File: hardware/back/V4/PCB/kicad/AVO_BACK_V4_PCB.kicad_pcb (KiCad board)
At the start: 4 copper layers, 46.7 x 47.4 mm, 105 parts, among them J1 USB-C 16P, J2 BATERÍA 1S, J3 microSD DM3AT, J4 URTK1.2 (8 hilos), Q1 AO3401A, Q2 AO3401A, Q3 AO3401A, Q4 AO3401A, U1 BQ51013BRHLR, U2 BQ24072RGTR, U3 TLV75733PDBVR, U4 ESP32-S3-MINI-1U-N8, U6 USBLC6-2SC6, U7 RT9080-33GJ5, U8 DRV5032FADBZR

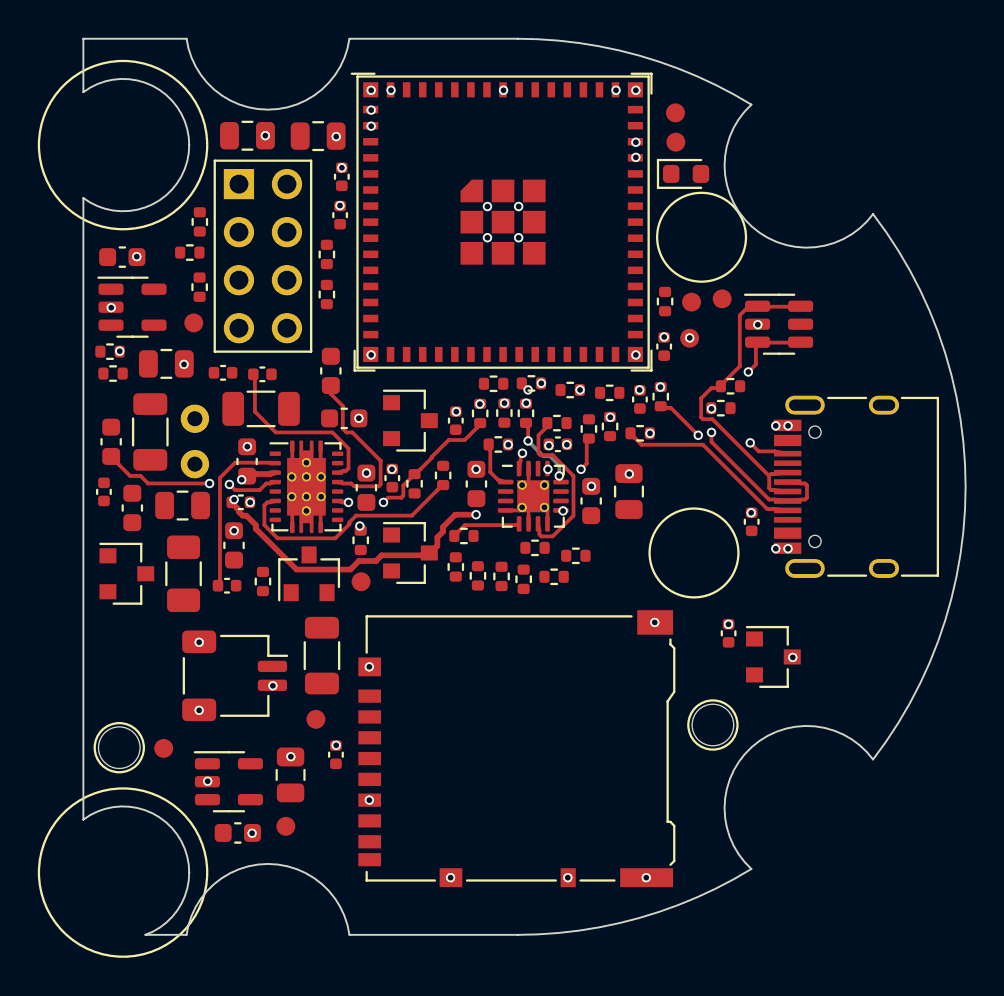
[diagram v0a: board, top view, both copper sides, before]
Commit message: PCB espalda V4: resultados de KiCad 9 de f2d8330 (puerta: false) [skip ci]
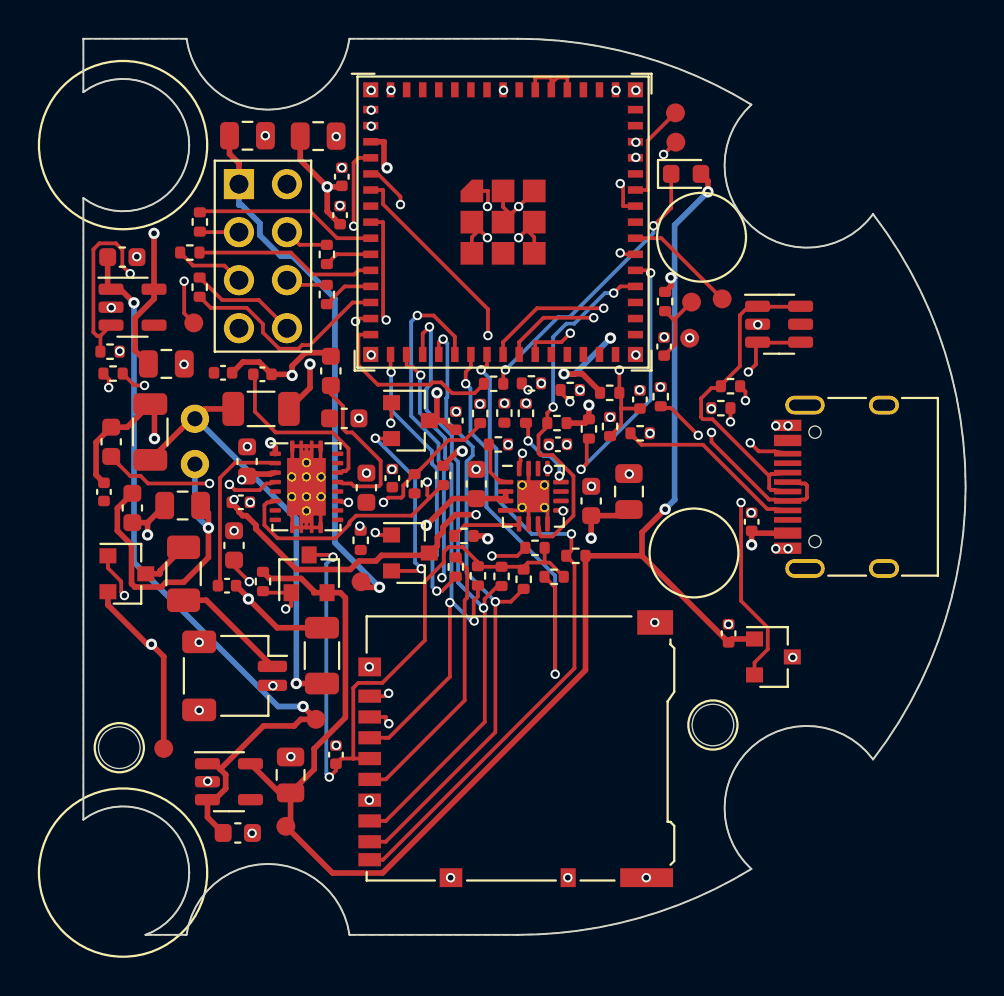
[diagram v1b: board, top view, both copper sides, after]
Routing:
- net +3V3: track 0.00 -> 136.9 mm, vias 0 -> 7
- net VBAT: track 0.00 -> 71.7 mm, vias 0 -> 4
- net VSYS: track 0.00 -> 65.0 mm, vias 0 -> 4
- net QI_AC1: track 0.00 -> 46.4 mm, vias 0 -> 5
- net +3V3_SD: track 0.00 -> 44.4 mm, vias 0 -> 3
- net HALL: track 0.00 -> 43.8 mm, vias 0 -> 2
- net +3V3_ZED: track 0.00 -> 41.9 mm, vias 0 -> 2
- net SD_PWR_N: track 0.00 -> 41.4 mm, vias 0 -> 2
- net SD_D3: track 0.00 -> 35.5 mm, vias 0 -> 3
- net SD_CD: track 0.00 -> 35.3 mm, vias 0 -> 2
- net BAT_G: track 0.00 -> 34.6 mm, vias 0 -> 2
- net SD_D1: track 0.00 -> 34.0 mm, vias 0 -> 2
- net SD_D0: track 0.00 -> 33.8 mm, vias 0 -> 2
- net SD_D2: track 0.00 -> 32.0 mm, vias 0 -> 4
- net QI_AC2: track 0.00 -> 30.5 mm, vias 0 -> 2
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- added copper zone on In2.Cu, net +3V3
- added copper zone on B.Cu, net GND
- added copper zone on F.Cu, net GND

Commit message: PCB espalda V4: resultados de KiCad 9 de 04e2e6f (puerta: false) [skip ci]
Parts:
- moved TP2 26.9 mm to (96.7, 81.8)
- moved TP9 22.9 mm to (99.4, 92.3)
- moved C62 20.8 mm to (90.1, 95.1)
- moved R47 17.9 mm to (79.0, 116.2), turned to 90 degrees
- moved R4 15.6 mm to (69.2, 99.5), turned to 0 degrees
- moved R2 15.5 mm to (74.8, 106.0), turned to 0 degrees
- moved TP7 15.0 mm to (67.0, 99.2)
- moved R54 14.3 mm to (81.3, 77.5)
- moved C8 14.0 mm to (80.7, 102.2)
- moved C61 12.7 mm to (74.2, 81.4)
- moved C11 12.7 mm to (80.0, 104.6), turned to 90 degrees
- moved C5 12.3 mm to (79.0, 95.2)
- moved C4 11.0 mm to (81.9, 99.6)
- moved C40 9.15 mm to (78.0, 111.2)
- moved RT1 9.06 mm to (85.8, 104.9), turned to 0 degrees
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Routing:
- net +3V3: track 136.9 -> 0.00 mm, vias 7 -> 0
- net VBAT: track 71.7 -> 0.00 mm, vias 4 -> 0
- net VSYS: track 65.0 -> 0.00 mm, vias 4 -> 0
- net QI_AC1: track 46.4 -> 0.00 mm, vias 5 -> 0
- net +3V3_SD: track 44.4 -> 0.00 mm, vias 3 -> 0
- net HALL: track 43.8 -> 0.00 mm, vias 2 -> 0
- net +3V3_ZED: track 41.9 -> 0.00 mm, vias 2 -> 0
- net SD_PWR_N: track 41.4 -> 0.00 mm, vias 2 -> 0
- net SD_D3: track 35.5 -> 0.00 mm, vias 3 -> 0
- net SD_CD: track 35.3 -> 0.00 mm, vias 2 -> 0
- net BAT_G: track 34.6 -> 0.00 mm, vias 2 -> 0
- net SD_D1: track 34.0 -> 0.00 mm, vias 2 -> 0
- net SD_D0: track 33.8 -> 0.00 mm, vias 2 -> 0
- net SD_D2: track 32.0 -> 0.00 mm, vias 4 -> 0
- net QI_AC2: track 30.5 -> 0.00 mm, vias 2 -> 0
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- removed copper zone on In2.Cu, net +3V3
- removed copper zone on B.Cu, net GND
- removed copper zone on F.Cu, net GND
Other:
- outline, holes or cut-outs redrawn

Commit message: PCB espalda V4: resultados de KiCad 9 de a08bbd6 (puerta: false) [skip ci]
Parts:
- moved TP2 26.9 mm to (71.5, 91.3)
- moved TP9 22.9 mm to (80.4, 105.0)
- moved C62 20.8 mm to (74.4, 81.4)
- moved R47 17.9 mm to (91.8, 103.7), turned to 0 degrees
- moved R4 15.6 mm to (84.7, 99.4), turned to 90 degrees
- moved R2 15.5 mm to (86.7, 96.1), turned to 90 degrees
- moved TP7 15.0 mm to (70.0, 113.8)
- moved R54 14.3 mm to (71.3, 87.6)
- moved C8 14.0 mm to (66.8, 100.3)
- moved C61 12.7 mm to (70.1, 93.5)
- moved C11 12.7 mm to (73.1, 94.0), turned to 0 degrees
- moved C5 12.3 mm to (68.3, 101.1)
- moved C4 11.0 mm to (71.0, 101.0)
- moved C40 9.15 mm to (73.7, 103.1)
- moved RT1 9.06 mm to (88.0, 96.1), turned to 90 degrees
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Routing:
- net +3V3: track 0.00 -> 138.4 mm, vias 0 -> 7
- net VSYS: track 0.00 -> 60.8 mm, vias 0 -> 4
- net +3V3_ZED: track 0.00 -> 55.7 mm, vias 0 -> 2
- net BAT_G: track 0.00 -> 52.8 mm, vias 0 -> 2
- net VBAT: track 0.00 -> 50.6 mm, vias 0 -> 3
- net VBUS: track 0.00 -> 49.6 mm, vias 0 -> 6
- net QI_AC2: track 0.00 -> 49.5 mm, vias 0 -> 1
- net SD_CD: track 0.00 -> 40.0 mm, vias 0 -> 3
- net QI_CHG: track 7.71 -> 46.6 mm, vias 0 -> 5
- net QI_AC1: track 0.00 -> 38.6 mm, vias 0 -> 3
- net HALL: track 0.00 -> 38.3 mm, vias 0 -> 3
- net +3V3_SD: track 0.00 -> 37.0 mm, vias 0 -> 2
- net SD_CLK0: track 0.00 -> 35.3 mm, vias 0 -> 4
- net SD_D3: track 0.00 -> 34.8 mm, vias 0 -> 4
- net SD_D1: track 0.00 -> 33.4 mm, vias 0 -> 2
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- added copper zone on In2.Cu, net +3V3
- added copper zone on B.Cu, net GND
- added copper zone on F.Cu, net GND

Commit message: PCB espalda V4: resultados de KiCad 9 de 7ee8318 (puerta: false) [skip ci]
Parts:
- moved C40 19.2 mm to (91.6, 96.3)
- moved TP9 17.0 mm to (67.1, 94.5)
- moved C7 15.3 mm to (78.8, 107.5), turned to -90 degrees
- moved R40 14.3 mm to (86.6, 96.4)
- moved C8 14.1 mm to (79.9, 105.4), turned to 0 degrees
- moved Q4 13.9 mm to (88.9, 96.5)
- moved C3 12.3 mm to (69.0, 101.0)
- moved TP7 11.8 mm to (66.9, 102.5)
- moved R55 11.6 mm to (78.5, 96.9), turned to 90 degrees
- moved R43 11.5 mm to (78.5, 109.7), turned to 0 degrees
- moved R41 11.1 mm to (75.6, 103.1)
- moved R53 9.59 mm to (76.7, 94.3)
- moved C11 8.54 mm to (81.5, 95.1), turned to 90 degrees
- moved R6 8.34 mm to (81.5, 97.2), turned to 90 degrees
- moved TP8 7.74 mm to (70.4, 113.9)
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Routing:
- net VBAT: track 50.6 -> 84.5 mm, vias 3 -> 7
- net VIN5: track 27.4 -> 60.1 mm, vias 3 -> 5
- net QI_AC2: track 49.5 -> 20.5 mm, vias 1 -> 2
- net +3V3_ZED: track 55.7 -> 28.2 mm, vias 2 -> 0
- net +3V3: track 138.4 -> 112.9 mm
- net SD_PWR_N: track 32.6 -> 7.59 mm
- net SD_CLK0: track 35.3 -> 18.7 mm, vias 4 -> 2
- net QI_CHG: track 46.6 -> 30.1 mm, vias 5 -> 3
- net +3V3_SD: track 37.0 -> 53.2 mm, vias 2 -> 5
- net QI_ADEN: track 22.2 -> 7.86 mm, vias 2 -> 0
- net BAT_G: track 52.8 -> 38.7 mm
- net QI_RECT: track 3.02 -> 16.2 mm, vias 0 -> 2
- net HALL: track 38.3 -> 49.6 mm, vias 3 -> 2
- net EN: track 16.1 -> 26.3 mm
- net CHG_STAT: track 17.4 -> 25.7 mm
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
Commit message: PCB espalda V4: resultados de KiCad 9 de 207f2bd (puerta: false) [skip ci]
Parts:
- moved R32 16.9 mm to (85.2, 77.5), turned to 0 degrees
- moved R6 12.9 mm to (94.3, 95.5)
- moved R42 11.2 mm to (78.3, 110.9)
- moved R4 9.60 mm to (93.1, 95.5), turned to 90 degrees
- moved R46 9.42 mm to (87.2, 104.8), turned to 90 degrees
- moved TP10 8.46 mm to (98.8, 80.8)
- moved C16 7.24 mm to (73.3, 103.8), turned to 90 degrees
- moved R41 7.09 mm to (78.4, 109.7), turned to 0 degrees
- moved R55 5.32 mm to (83.2, 94.6), turned to 0 degrees
- moved TP1 4.88 mm to (101.5, 88.7)
- moved R33 4.54 mm to (97.1, 90.2), turned to 0 degrees
- moved RT2 4.32 mm to (96.6, 91.8)
- moved R9 3.55 mm to (94.5, 100.8), turned to 0 degrees
- moved R16 3.17 mm to (96.7, 98.7), turned to 90 degrees
- moved C15 3.12 mm to (74.8, 104.4), turned to 90 degrees
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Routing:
- net VIN5: track 60.1 -> 18.0 mm, vias 5 -> 3
- net VBAT: track 84.5 -> 59.5 mm, vias 7 -> 4
- net USB_DM: track 19.0 -> 0.00 mm, vias 2 -> 0
- net ZED_PPS: track 16.2 -> 0.00 mm, vias 2 -> 0
- net +3V3_SD: track 53.2 -> 38.9 mm, vias 5 -> 3
- net BAT_ADC: track 27.2 -> 40.9 mm
- net +3V3: track 112.9 -> 125.6 mm
- net VBUS: track 42.2 -> 32.1 mm
- net QI_AC1: track 38.8 -> 28.9 mm, vias 2 -> 0
- net LED: track 16.0 -> 6.97 mm
- net HALL: track 49.6 -> 41.6 mm
- net CHG_TS: track 7.67 -> 15.3 mm, vias 2 -> 0
- net SD_CMD: track 34.3 -> 27.1 mm, vias 4 -> 2
- net CHG_STAT: track 25.7 -> 18.6 mm, vias 3 -> 2
- net CHG_ILIM: track 0.00 -> 6.84 mm
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
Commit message: PCB espalda V4: resultados de KiCad 9 de 3f81b45 (puerta: true) [skip ci]
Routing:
- net +3V3: track 125.6 -> 99.1 mm, vias 7 -> 11
- net VIN5: track 18.0 -> 39.0 mm, vias 3 -> 7
- net CHG_TS: track 15.3 -> 36.2 mm, vias 0 -> 8
- net CHG_ISET: track 9.67 -> 27.7 mm, vias 0 -> 2
- net USB_DM: track 0.00 -> 14.3 mm
- net VBUS: track 32.1 -> 44.9 mm
- net QI_COIL1: track 20.6 -> 8.53 mm, vias 1 -> 3
- net ZED_PPS: track 0.00 -> 12.0 mm, vias 0 -> 2
- net SD_PWR_N: track 13.8 -> 5.36 mm, vias 3 -> 2
- net VSYS: track 71.2 -> 76.2 mm, vias 5 -> 8
- net SD_CD: track 41.3 -> 36.9 mm, vias 2 -> 4
- net BAT_G: track 38.9 -> 35.6 mm
- net VBAT: track 59.5 -> 61.9 mm, vias 4 -> 8
- net USB_DP_C: track 18.0 -> 20.4 mm, vias 0 -> 2
- net QI_CHG: track 28.8 -> 30.7 mm, vias 3 -> 4

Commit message: PCB espalda V4: resultados de KiCad 9 de eca125a (puerta: false) [skip ci]
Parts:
- removed C1, C2: 100n C0G 50V, AVO:C_1206_3216Metric
- removed C10, C7: 470n 25V, AVO:C_0603_1608Metric
- removed C11, C8: 22n 50V, AVO:C_0402_1005Metric
- removed C12, C13, C15: 10u 25V, AVO:C_0603_1608Metric
- removed C14, C16, C33: 100n, AVO:C_0402_1005Metric
- removed C17: 1u, AVO:C_0402_1005Metric
- removed C3: 47n C0G 50V, AVO:C_1206_3216Metric
- removed C4: 2n2 C0G 50V, AVO:C_0805_2012Metric
- removed C5: 1n C0G 50V, AVO:C_0603_1608Metric
- removed C6, C9: 10n 50V, AVO:C_0402_1005Metric
- removed L1: BOBINA Qi (1), AVO:WirePad_D1.5_Drill0.8
- removed L2: BOBINA Qi (2), AVO:WirePad_D1.5_Drill0.8
- removed Q1, Q2: AO3401A, AVO:SOT-23
- removed R1: 330R, AVO:R_0402_1005Metric
- removed R2: 200R, AVO:R_0402_1005Metric
- removed R3: 20k, AVO:R_0402_1005Metric
- removed R4: 100k, AVO:R_0402_1005Metric
- removed RT1: NTC 10k B3380, AVO:R_0402_1005Metric
- removed U1: BQ51013BRHLR, AVO:Texas_VQFN-RHL-20_ThermalVias
- removed U8: DRV5032FADBZR, AVO:SOT-23
- added D2: TVS 5 V, AVO:D_SOD-323, F.Cu at (99.8, 99.9)
- added D3: TVS 5 V, AVO:D_SOD-323, F.Cu at (99.8, 97.7)
- added P1: CONTACTO SYS, AVO:AVO_Contacto_M2_Tornillo, F.Cu at (101.0, 108.6)
- added P2: CONTACTO BAT, AVO:AVO_Contacto_M2_Tornillo, F.Cu at (106.8, 108.6)
- added P3: CONTACTO GND, AVO:AVO_Contacto_M2_Tornillo, F.Cu at (80.0, 100.0)
- moved Q3 25.9 mm to (93.7, 103.8), turned to 0 degrees
- moved TP7 24.3 mm to (91.1, 104.0)
- moved R32 17.4 mm to (82.3, 94.6)
- moved R47 15.9 mm to (77.8, 103.7)
- moved R33 13.6 mm to (84.7, 95.8)
- moved TP3 13.1 mm to (82.7, 96.0)
- moved C34 11.5 mm to (86.9, 96.8), turned to 0 degrees
- moved R7 10.5 mm to (85.0, 94.6), turned to 0 degrees
- moved RT2 10.0 mm to (87.3, 95.6), turned to 0 degrees
- moved R45 9.72 mm to (84.4, 99.3), turned to 0 degrees
- moved R53 9.59 mm to (71.9, 86.0)
- moved R54 9.46 mm to (76.3, 93.7)
- moved TP10 9.45 mm to (99.4, 90.2)
- moved C40 9.28 mm to (86.4, 104.0)
- moved Q4 9.07 mm to (83.8, 104.0), turned to 0 degrees
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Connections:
- C18 pad 1: VIN5 -> VBUS
- Q3 pad 3: BAT_F -> SYS_IN
- U2 pad 13: VIN5 -> VBUS
- U4 pad 36: QI_CHG -> unconnected-(U4-IO40-Pad36)
- U4 pad 5: HALL -> unconnected-(U4-IO1-Pad5)
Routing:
- net VBAT: track 61.9 -> 20.1 mm, vias 8 -> 2
- net HALL: track 41.6 -> 0.00 mm, vias 2 -> 0
- net BAT_F: track 4.46 -> 44.8 mm, vias 0 -> 2
- net VIN5: track 39.0 -> 0.00 mm, vias 7 -> 0
- net CHG_TS: track 36.2 -> 4.65 mm, vias 8 -> 2
- net QI_CHG: track 30.7 -> 0.00 mm, vias 4 -> 0
- net QI_AC1: track 28.9 -> 0.00 mm
- net BAT_G: track 35.6 -> 9.15 mm
- net +3V3: track 99.1 -> 124.8 mm, vias 11 -> 6
- net BAT_ADC: track 40.9 -> 16.8 mm
- net CHG_ISET: track 27.7 -> 4.56 mm
- net VBUS: track 44.9 -> 21.7 mm, vias 3 -> 2
- net SYS_IN: track 0.00 -> 19.5 mm, vias 0 -> 1
- net QI_AC2: track 19.3 -> 0.00 mm
- net LED_K: track 17.7 -> 0.00 mm, vias 2 -> 0
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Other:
- board text added: "AVO BACK V4 · REV B · ESP32-S3 · 2026-10-30"
- board text added: "BAT"
- board text added: "GND"
- board text added: "SYS"
- board text removed: "AVO BACK V4 · REV A · ESP32-S3 · 2026-10-29"
- board text removed: "BOBINA Qi DEBAJO"

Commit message: PCB espalda V4: resultados de KiCad 9 de c1e0e26 (puerta: true) [skip ci]
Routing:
- net +3V3: track 124.8 -> 99.8 mm, vias 6 -> 9
- net CHG_ILIM: track 12.0 -> 34.8 mm, vias 0 -> 6
- net SD_CLK: track 0.00 -> 16.8 mm, vias 0 -> 2
- net USB_DP: track 0.00 -> 16.6 mm, vias 0 -> 3
- net USB_DM: track 0.00 -> 15.5 mm, vias 0 -> 3
- net LED_K: track 0.00 -> 14.4 mm, vias 0 -> 4
- net VBUS: track 21.7 -> 31.8 mm, vias 2 -> 3
- net CHG_PG: track 26.8 -> 18.1 mm, vias 2 -> 5
- net VSYS: track 68.6 -> 61.3 mm, vias 4 -> 12
- net SD_D3: track 25.2 -> 30.5 mm, vias 3 -> 5
- net SD_CMD: track 37.0 -> 36.1 mm
- net BAT_ADC: track 16.8 -> 16.1 mm
- net +3V3_SD: track 42.2 -> 42.6 mm, vias 5 -> 7
- net SD_D2: track 25.8 -> 25.7 mm, vias 3 -> 5
- net VBAT: vias 2 -> 3
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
